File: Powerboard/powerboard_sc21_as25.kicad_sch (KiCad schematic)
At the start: 44 parts, among them J10 Conn_01x04_Male, J2 Conn_01x02_Male, J3 Conn_01x02_Male, J4 Conn_01x08_Male, J9 Conn_Coaxial, Q6 MMDT2222A, Q7 RSJ250P10TL, Q8 RSJ250P10TL, U1 LTC4412xS6, U2 SN65HVD230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

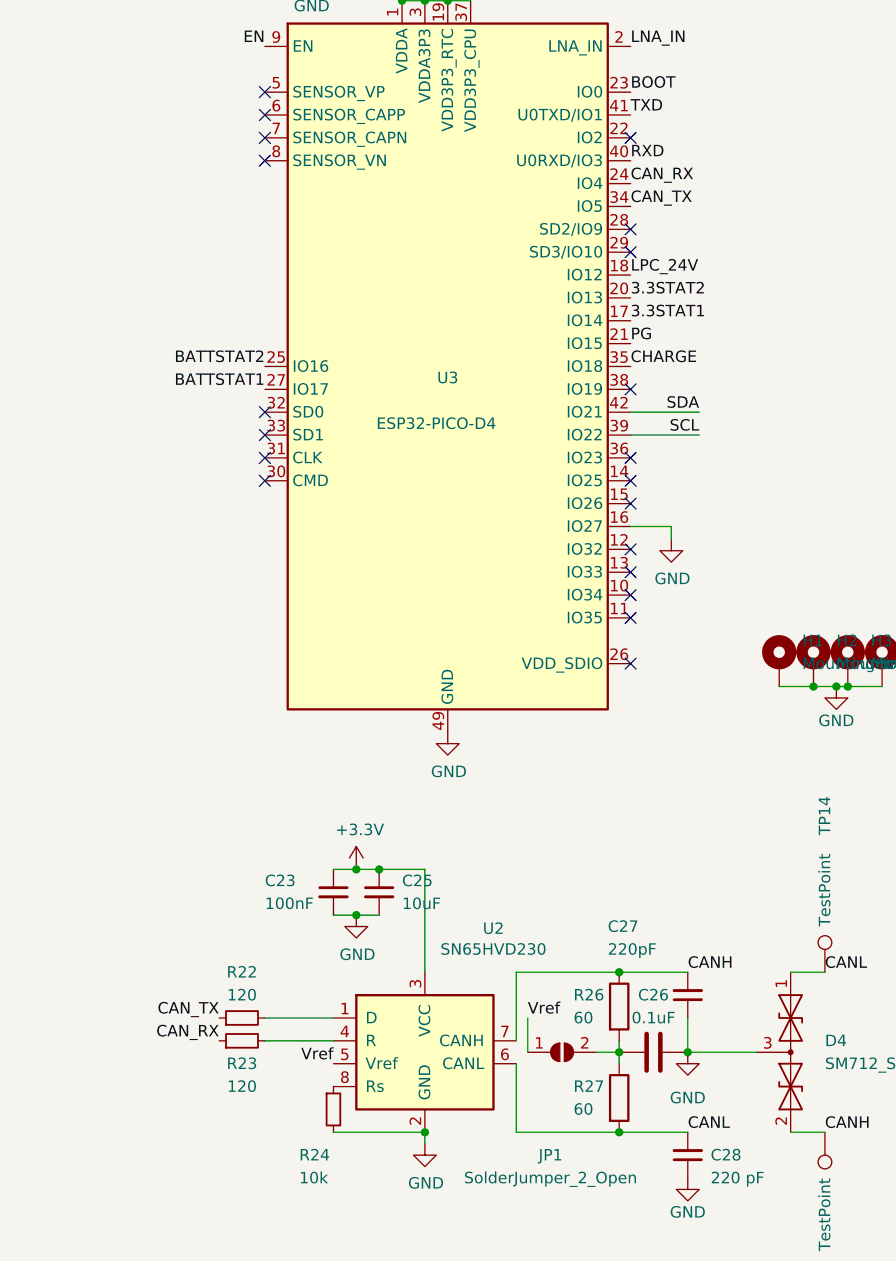
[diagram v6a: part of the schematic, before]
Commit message: Removed CAN resistors
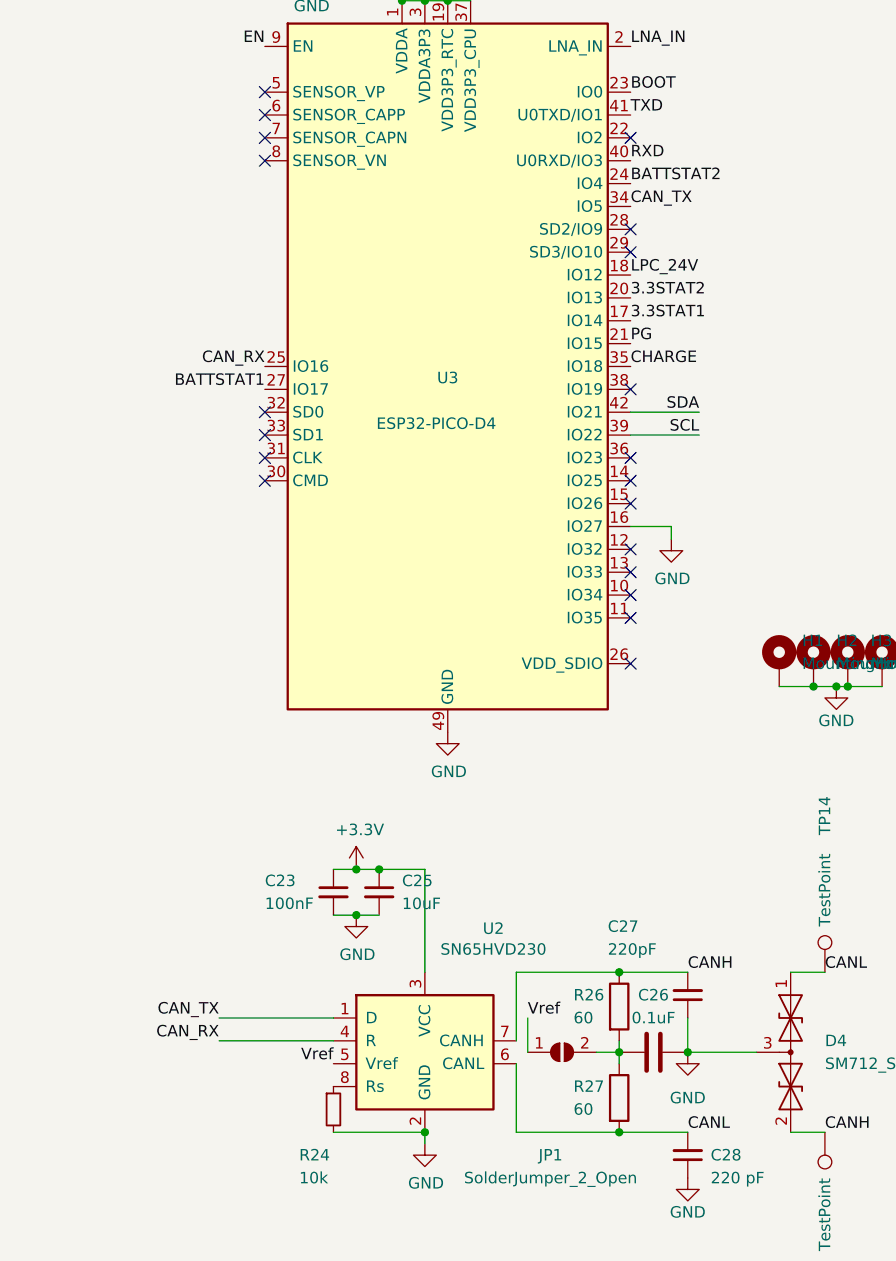
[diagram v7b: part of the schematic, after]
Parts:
- removed R22, R23: 120, Resistor_SMD:R_0603_1608Metric, symbol Device:R_Small
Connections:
- net BATTSTAT2: now also U3.24 (IO4); no longer U3.25 (IO16)
- net CAN_RX: now also U2.4 (R), U3.25 (IO16); no longer U3.24 (IO4)
- net CAN_TX: now also U2.1 (D)
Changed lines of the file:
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@@
     (stroke (width 0) (type default) (color 0 0 0 0))
   )
-  (wire (pts (xy 196.85 146.05) (xy 204.47 146.05))
+  (wire (pts (xy 191.77 146.05) (xy 204.47 146.05))
     (stroke (width 0) (type default) (color 0 0 0 0))
   )
@@
     (stroke (width 0) (type default) (color 0 0 0 0))
   )
-  (wire (pts (xy 196.85 148.59) (xy 204.47 148.59))
+  (wire (pts (xy 191.77 148.59) (xy 204.47 148.59))
     (stroke (width 0) (type default) (color 0 0 0 0))
   )
@@
     (effects (font (size 1.27 1.27)) (justify left bottom))
   )
+  (label "BATTSTAT2" (at 237.49 53.34 0)
+    (effects (font (size 1.27 1.27)) (justify left bottom))
+  )
   (label "DTR" (at 69.85 173.99 0)
     (effects (font (size 1.27 1.27)) (justify left bottom))
@@
     (effects (font (size 1.27 1.27)) (justify left bottom))
   )
+  (label "CAN_RX" (at 196.85 73.66 180)
+    (effects (font (size 1.27 1.27)) (justify right bottom))
+  )
   (label "BOOT" (at 62.23 46.99 0)
     (effects (font (size 1.27 1.27)) (justify left bottom))
@@
     (effects (font (size 1.27 1.27)) (justify left bottom))
   )
-  (label "CAN_RX" (at 237.49 53.34 0)
-    (effects (font (size 1.27 1.27)) (justify left bottom))
-  )
   (label "BOOT" (at 85.09 82.55 0)
     (effects (font (size 1.27 1.27)) (justify left bottom))
@@
   )
   (label "TXD" (at 144.78 41.91 180)
-    (effects (font (size 1.27 1.27)) (justify right bottom))
-  )
-  (label "BATTSTAT2" (at 196.85 73.66 180)
     (effects (font (size 1.27 1.27)) (justify right bottom))
   )
@@
     (pin "5")
   )
-  (symbol (lib_id "Device:R_Small") (at 194.31 148.59 90) (unit 1)
-    (in_bom yes) (on_board yes)
-    (property "Reference" "R23" (id 0) (at 194.31 151.13 90))
-    (property "Value" "120" (id 1) (at 194.31 153.67 90))
-    (property "Footprint" "Resistor_SMD:R_0603_1608Metric" (id 2) (at 194.31 148.59 0)
-      (effects (font (size 1.27 1.27)) hide)
-    )
-    (property "Datasheet" "~" (id 3) (at 194.31 148.59 0)
-      (effects (font (size 1.27 1.27)) hide)
-    )
-    (pin "1")
-    (pin "2")
-  )
   (symbol (lib_id "power:GND") (at 144.78 64.77 0) (unit 1)
     (in_bom yes) (on_board yes)
@@
     )
     (pin "1")
-  )
-  (symbol (lib_id "Device:R_Small") (at 194.31 146.05 90) (unit 1)
-    (in_bom yes) (on_board yes)
-    (property "Reference" "R22" (id 0) (at 194.31 140.97 90))
-    (property "Value" "120" (id 1) (at 194.31 143.51 90))
-    (property "Footprint" "Resistor_SMD:R_0603_1608Metric" (id 2) (at 194.31 146.05 0)
-      (effects (font (size 1.27 1.27)) hide)
-    )
-    (property "Datasheet" "~" (id 3) (at 194.31 146.05 0)
-      (effects (font (size 1.27 1.27)) hide)
-    )
-    (pin "1")
-    (pin "2")
   )
   (symbol (lib_id "iclr:RSJ250P10TL") (at 157.607 102.997 180) (unit 1)
@@
       (reference "R21") (unit 1) (value "470") (footprint "Resistor_SMD:R_0603_1608Metric")
     )
-    (path "/987a1960-bbf6-4216-bbcb-8e7298a0186d"
-      (reference "R22") (unit 1) (value "120") (footprint "Resistor_SMD:R_0603_1608Metric")
-    )
-    (path "/627a37e5-d010-4b2c-911f-330978d69979"
-      (reference "R23") (unit 1) (value "120") (footprint "Resistor_SMD:R_0603_1608Metric")
-    )
     (path "/367b9243-e298-4361-927a-ff1499c679d9"

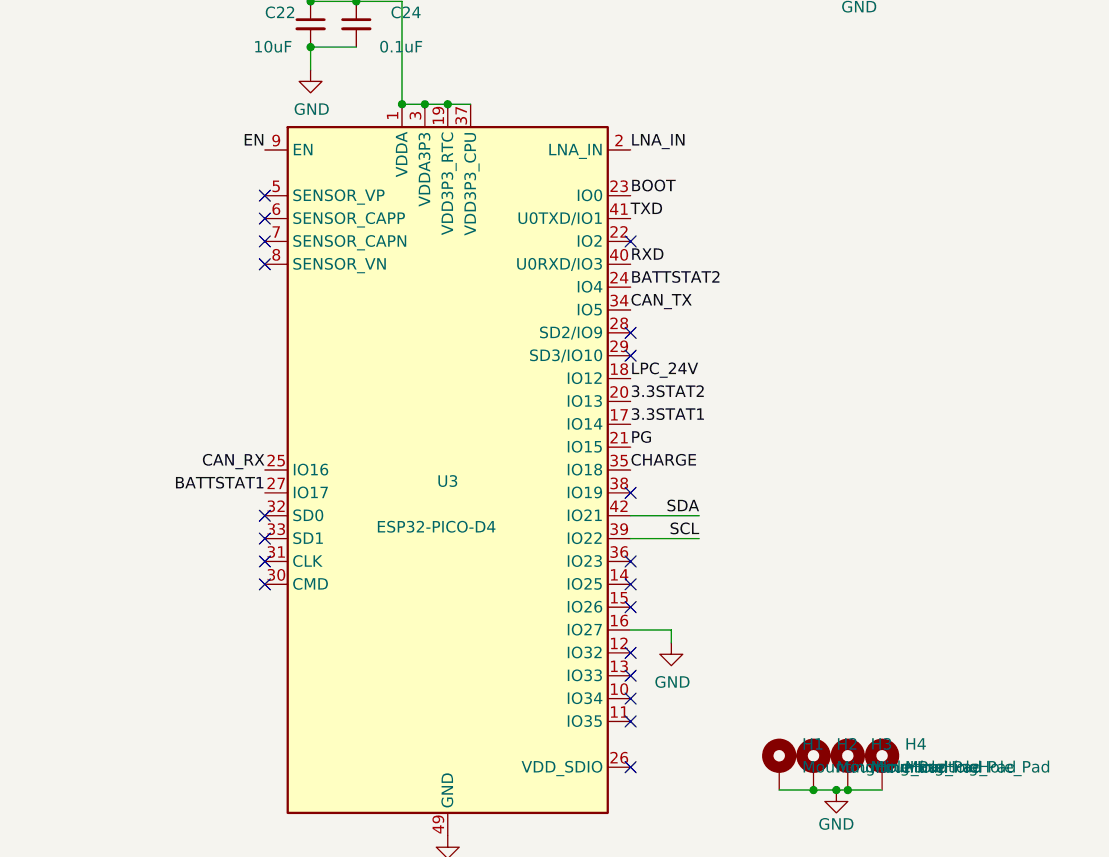
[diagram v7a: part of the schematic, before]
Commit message: Added connector for PDU EN pin and external LED + routing changes
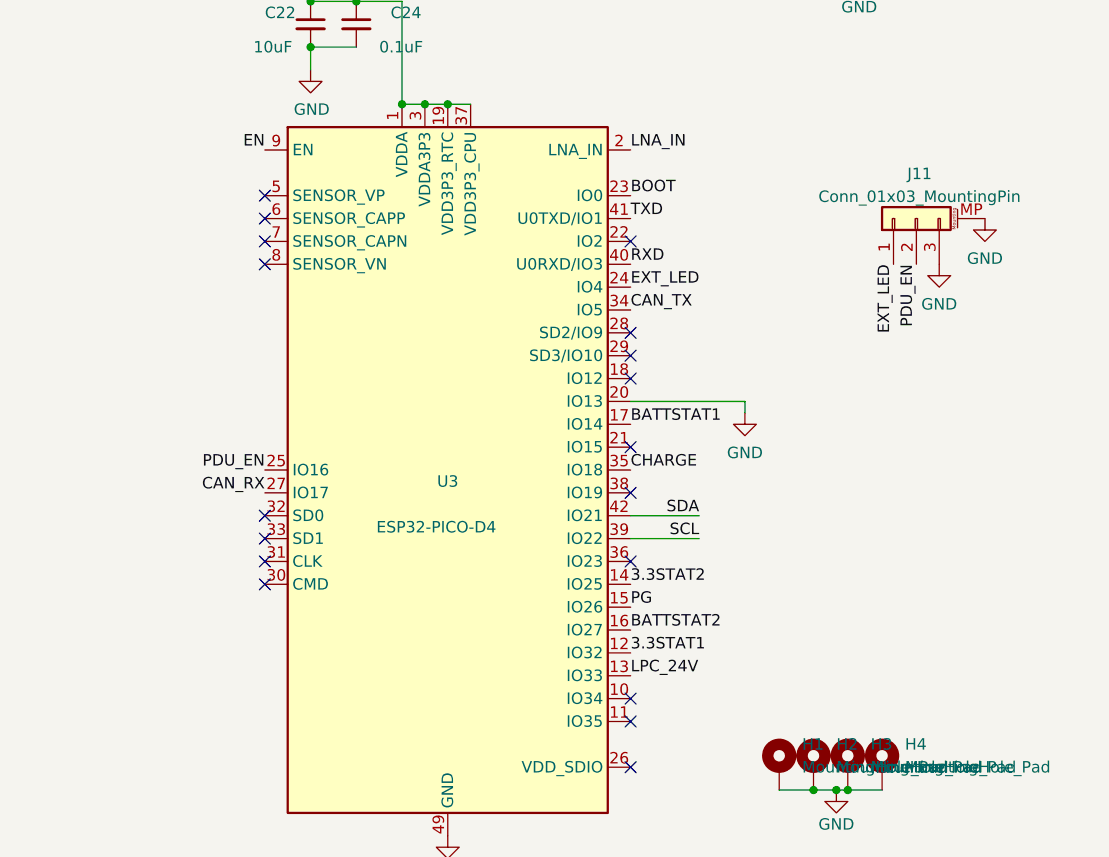
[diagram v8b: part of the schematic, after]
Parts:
- added J11: Conn_01x03_MountingPin, Connector_Molex:Molex_PicoBlade_53261-0371_1x03-1MP_P1.25mm_Horizontal, symbol Connector_Generic_MountingPin:Conn_01x03_MountingPin
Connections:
- net 3.3STAT1: now also U3.12 (IO32); no longer U3.17 (IO14)
- net 3.3STAT2: now also U3.14 (IO25); no longer U3.20 (IO13)
- net BATTSTAT1: now also U3.17 (IO14); no longer U3.27 (IO17)
- net BATTSTAT2: now also U3.16 (IO27); no longer U3.24 (IO4)
- net CAN_RX: now also U3.27 (IO17); no longer U3.25 (IO16)
- net GND: now also U3.20 (IO13), J11.3 (Pin_3), J11.MP (MountPin); no longer U3.16 (IO27)
- net LPC_24V: now also U3.13 (IO33); no longer U3.18 (IO12)
- net PG: now also U3.15 (IO26); no longer U3.21 (IO15)
- new net EXT_LED: J11.1 (Pin_1), U3.24 (IO4)
- new net PDU_EN: J11.2 (Pin_2), U3.25 (IO16)
- no-connect marks 21 -> 19
